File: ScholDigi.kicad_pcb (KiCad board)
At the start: 2 copper layers, 66 x 49 mm, 65 parts, among them J1 Conn_01x04, J2 USB_C_Receptacle_USB2.0_14P, J3 Battery JST, J4 GPS Antenna coaxial, J5 USB_C_Receptacle_USB2.0_14P, Q1 FS8205A, SW1 Boot Button, SW2 Reset Button, U1 ESP32-C6-MINI-1, U2 MAX-M10S, U3 TP4056-42-ESOP8, U4 DW01A, U5 TPS63060, U6 CP2102

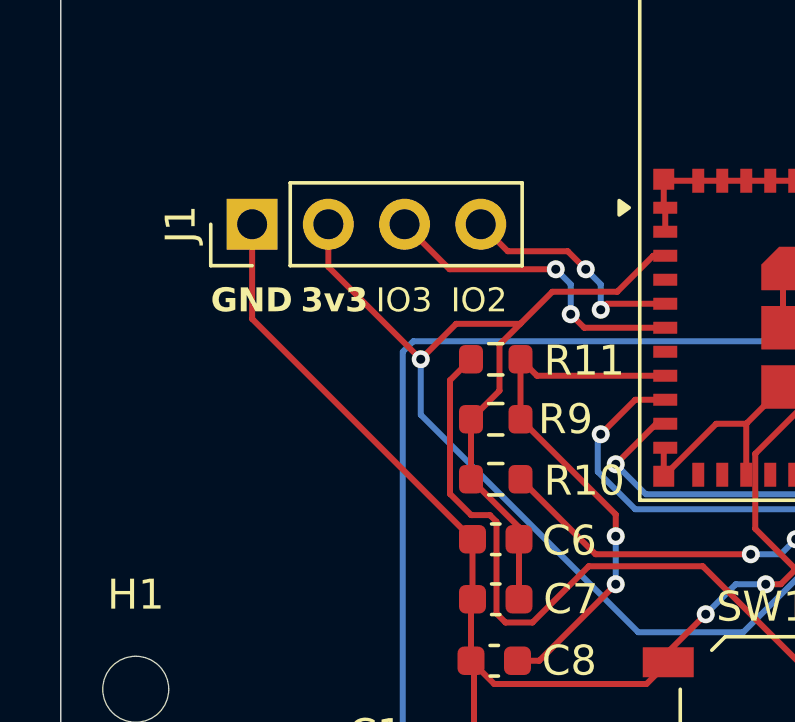
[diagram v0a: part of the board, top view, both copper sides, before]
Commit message: Display header are now through hole solders
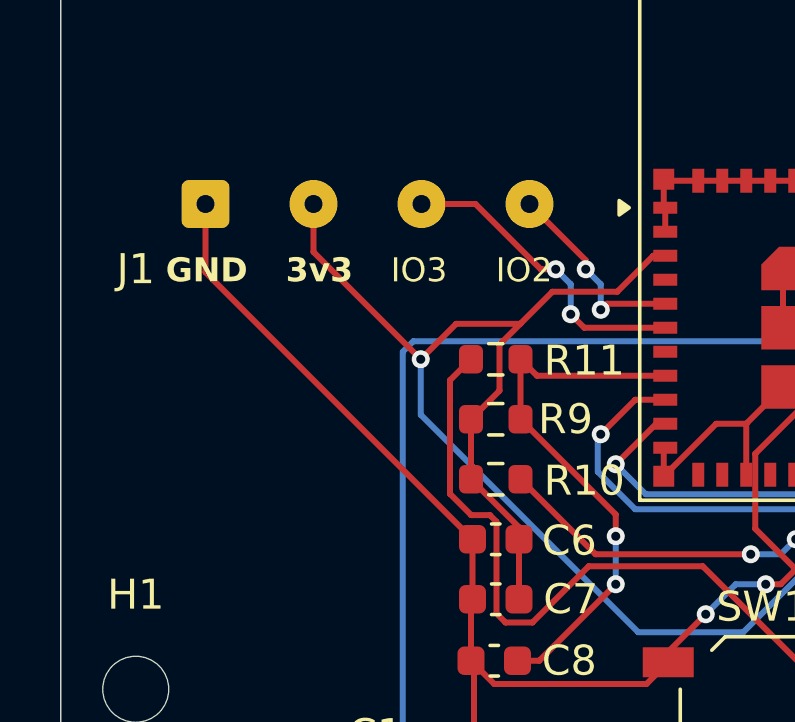
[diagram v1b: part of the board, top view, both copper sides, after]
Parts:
- J1: footprint Connector_PinHeader_2.54mm:PinHeader_1x04_P2.54mm_Vertical -> Connector_Wire:SolderWire-0.1sqmm_1x04_P3.6mm_D0.4mm_OD1mm
- moved J1 1.70 mm to (95.8, 59.3), turned to 0 degrees
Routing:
- net VIN-: track 345.2 -> 346.5 mm
- net IO2: track 7.91 -> 6.74 mm
- net +3V3: track 106.5 -> 107.4 mm

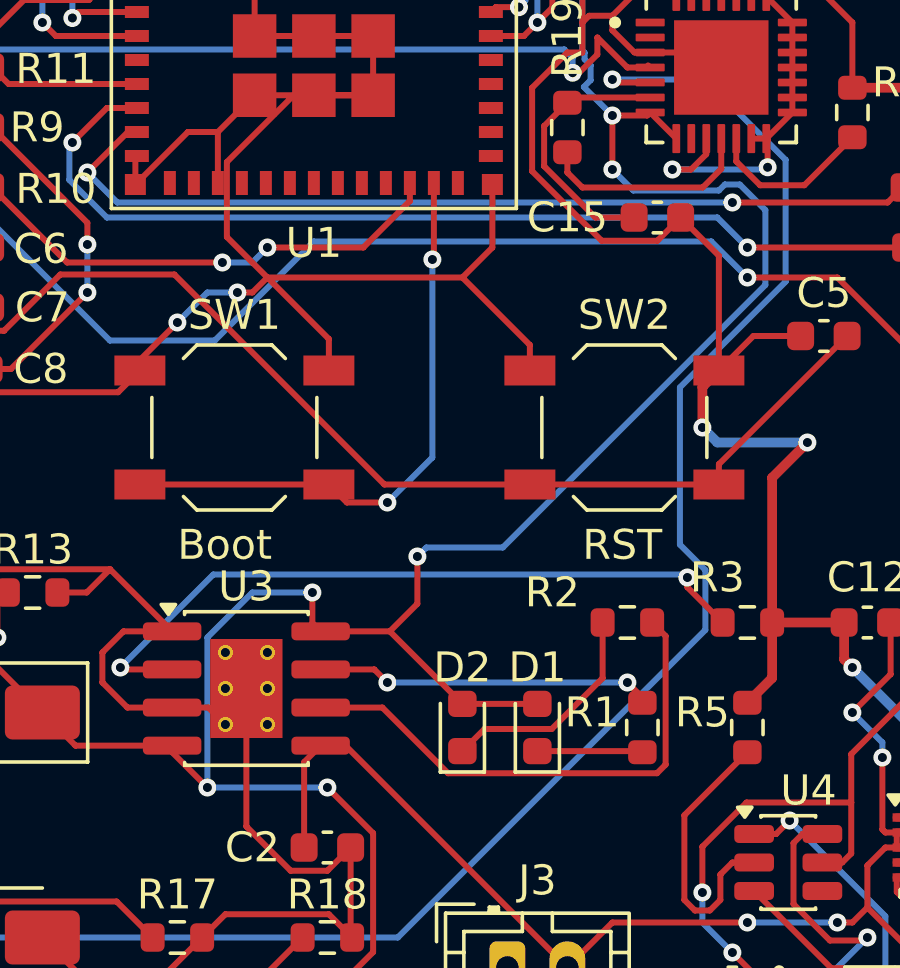
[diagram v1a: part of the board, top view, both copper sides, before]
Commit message: CHanges so that i can get battery voltage
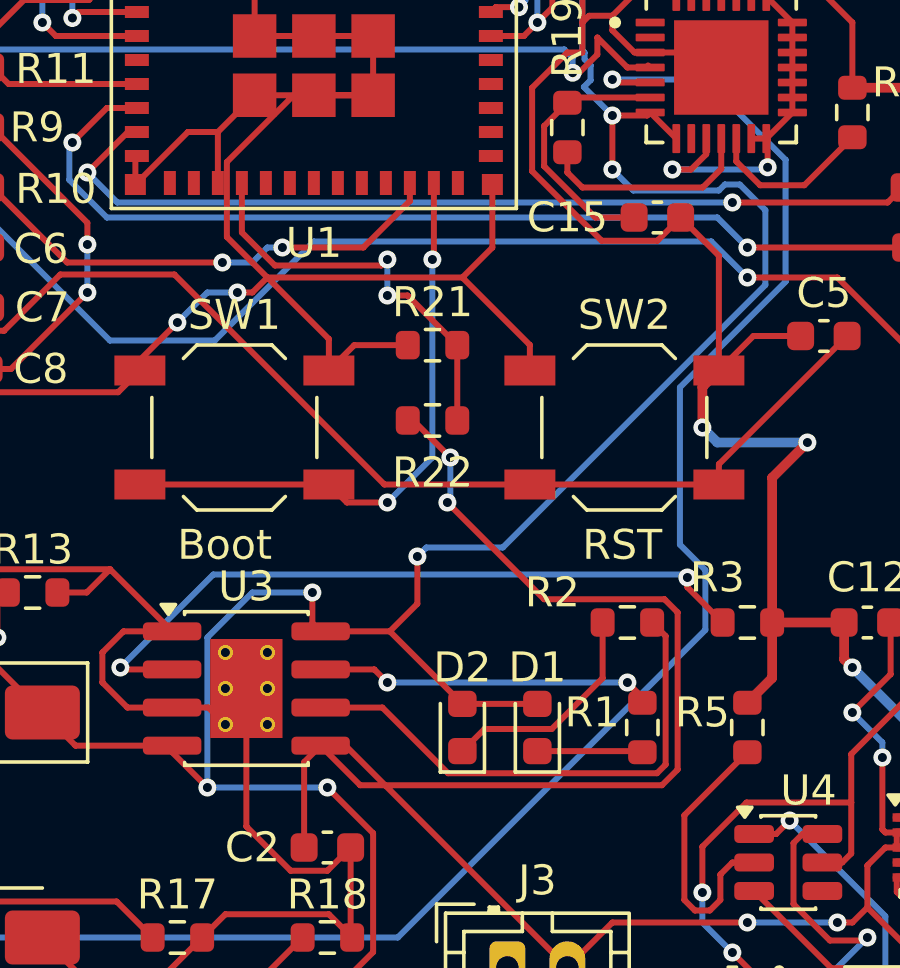
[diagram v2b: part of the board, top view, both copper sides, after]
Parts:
- added R21: 90K, Resistor_SMD:R_0603_1608Metric, F.Cu at (121.0, 73.8)
- added R22: 10K, Resistor_SMD:R_0603_1608Metric, F.Cu at (121.0, 76.3)
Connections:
- U1 pad 15: unconnected-(U1-IO6-Pad15) -> Net-(U1-IO6)
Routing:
- net BAT+: track 53.2 -> 83.8 mm, vias 4 -> 6
- net Net-(U1-IO6): track 0.00 -> 13.8 mm, vias 0 -> 2
- net VIN-: track 346.5 -> 349.5 mm

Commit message: rah
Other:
- board text added: "Anything can be a smoke machine if you try hard enough"
- board text added: "Now with 50% more magic smoke"
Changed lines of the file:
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@@
 		)
 	)
+	(gr_text "Now with 50% more magic smoke"
+		(at 121 64 0)
+		(layer "B.SilkS")
+		(effects
+			(font
+				(size 1.15 1.15)
+				(thickness 0.1)
+			)
+			(justify left bottom mirror)
+		)
+	)
+	(gr_text "Anything can be a smoke machine if you try hard enough"
+		(at 150 100.5 0)
+		(layer "B.SilkS")
+		(effects
+			(font
+				(size 1.25 1.25)
+				(thickness 0.1)
+			)
+			(justify left bottom mirror)
+		)
+	)
 	(segment
 		(start 103.565256 84)
@@
 	)
 	(segment
+		(start 120.175 72.1)
+		(end 119.5 72.1)
+		(width 0.2)
+		(layer "F.Cu")
+		(net "Net-(U1-IO6)")
+	)
+	(segment
+		(start 119.3 71.1)
+		(end 115.751471 71.1)
+		(width 0.2)
+		(layer "F.Cu")
+		(net "Net-(U1-IO6)")
+	)
+	(segment
+		(start 121.83 73.755)
+		(end 121.83 76.265)
+		(width 0.2)
+		(layer "F.Cu")
+		(net "Net-(U1-IO6)")
+	)
+	(segment
+		(start 121.83 73.755)
+		(end 120.175 72.1)
+		(width 0.2)
+		(layer "F.Cu")
+		(net "Net-(U1-IO6)")
+	)
+	(segment
+		(start 114.65 69.998529)
+		(end 114.65 68.35)
+		(width 0.2)
+		(layer "F.Cu")
+		(net "Net-(U1-IO6)")
+	)
+	(segment
+		(start 119.5 70.9)
+		(end 119.3 71.1)
+		(width 0.2)
+		(layer "F.Cu")
+		(net "Net-(U1-IO6)")
+	)
+	(segment
+		(start 115.751471 71.1)
+		(end 114.65 69.998529)
+		(width 0.2)
+		(layer "F.Cu")
+		(net "Net-(U1-IO6)")
+	)
+	(via
+		(at 119.5 72.1)
+		(size 0.6)
+		(drill 0.3)
+		(layers "F.Cu" "B.Cu")
+		(net "Net-(U1-IO6)")
+	)
+	(via
+		(at 119.5 70.9)
+		(size 0.6)
+		(drill 0.3)
+		(layers "F.Cu" "B.Cu")
+		(net "Net-(U1-IO6)")
+	)
+	(segment
+		(start 119.5 72.1)
+		(end 119.5 70.9)
+		(width 0.2)
+		(layer "B.Cu")
+		(net "Net-(U1-IO6)")
+	)
+	(segment
 		(start 128.225 60)
 		(end 127 60)
@@
 		(net "unconnected-(J2-SHIELD-PadSH)")
 	)
-	(segment
-		(start 120.175 72.1)
-		(end 119.5 72.1)
-		(width 0.2)
-		(layer "F.Cu")
-		(net "Net-(U1-IO6)")
-	)
-	(segment
-		(start 119.3 71.1)
-		(end 115.751471 71.1)
-		(width 0.2)
-		(layer "F.Cu")
-		(net "Net-(U1-IO6)")
-	)
-	(segment
-		(start 121.83 73.755)
-		(end 121.83 76.265)
-		(width 0.2)
-		(layer "F.Cu")
-		(net "Net-(U1-IO6)")
-	)
-	(segment
-		(start 121.83 73.755)
-		(end 120.175 72.1)
-		(width 0.2)
-		(layer "F.Cu")
-		(net "Net-(U1-IO6)")
-	)
-	(segment
-		(start 114.65 69.998529)
-		(end 114.65 68.35)
-		(width 0.2)
-		(layer "F.Cu")
-		(net "Net-(U1-IO6)")
-	)
-	(segment
-		(start 119.5 70.9)
-		(end 119.3 71.1)
-		(width 0.2)
-		(layer "F.Cu")
-		(net "Net-(U1-IO6)")
-	)
-	(segment
-		(start 115.751471 71.1)
-		(end 114.65 69.998529)
-		(width 0.2)
-		(layer "F.Cu")
-		(net "Net-(U1-IO6)")
-	)
-	(via
-		(at 119.5 72.1)
-		(size 0.6)
-		(drill 0.3)
-		(layers "F.Cu" "B.Cu")
-		(net "Net-(U1-IO6)")
-	)
-	(via
-		(at 119.5 70.9)
-		(size 0.6)
-		(drill 0.3)
-		(layers "F.Cu" "B.Cu")
-		(net "Net-(U1-IO6)")
-	)
-	(segment
-		(start 119.5 72.1)
-		(end 119.5 70.9)
-		(width 0.2)
-		(layer "B.Cu")
-		(net "Net-(U1-IO6)")
-	)
 	(embedded_fonts no)

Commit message: add funnies
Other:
- board text added: "Any sufficiently advanced technology is indistinguishable from magic - Arthur C Clark"
- board text added: "BAT"
- board text added: "Hi Pookie <3"
- board text added: "It is by pure will alone I set myself to this task"
- board text added: "Made in China"
- board text added: "Peekabooo"
- board text added: "Pineapple on pizza is gods creation"
- board text added: "Please do not the cat."
- board text added: "Remove before flight."
- board text added: "Schrödinger's PCB"
- board text added: "[Verse 1: David Gilmour] Ticking away The moments that make up a dull day You fritter and waste the hours In an offhand way Kicking around on a piece of ground In your hometown Waiting for someone Or something to show you the way [Chorus: Richard Wright] Tired of lying in the sunshine Staying home to watch the rain You are young and life is long And there is time to kill today And then one day yo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"
- board text added: "Привіт світ"
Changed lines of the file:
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@@
+		)
+	)
+	(gr_text "BAT"
+		(at 123 99.5 0)
+		(layer "F.SilkS")
+		(effects
+			(font
+				(size 1 1)
+				(thickness 0.1)
+			)
+			(justify left bottom)
 		)
 	)
@@
 		)
 	)
+	(gr_text "[Verse 1: David Gilmour]\nTicking away\nThe moments that make up a dull day\nYou fritter and waste the hours\nIn an offhand way\nKicking around on a piece of ground\nIn your hometown\nWaiting for someone\nOr something to show you the way\n\n[Chorus: Richard Wright]\nTired of lying in the sunshine\nStaying home to watch the rain\nYou are young and life is long\nAnd there is time to kill today\nAnd then one day you find\nTen years have got behind you\nNo one told you when to run\nYou missed the starting gun\nYou might also like\nmeet the grahams\nKendrick Lamar\nEclipse\nPink Floyd\nTHE HEART PART 6\nDrake\n[Guitar Solo]\n\n[Verse 2: David Gilmour]\nAnd you run, and you run\nTo catch up with the sun, but it's sinking\nAnd racing around\nTo come up behind you again\nThe sun is the same in a relative way\nBut you're older\nShorter of breath\nAnd one day closer to death\n\n[Chorus: Richard Wright]\nEvery year is getting shorter\nNever seem to find the time\nPlans that either come to naught\nOr half a page of scribbled lines\nHanging on in quiet desperation\nIs the English way\nThe time is gone, the song is over\nThought I'd something more to say\n\n[Part II: Breathe (In the Air) [Reprise]]\n\n[Verse: David Gilmour]\nHome, home again\nI like to be here when I can\nWhen I come home cold and tired\nIt's good to warm my bones beside the fire\nFar away across the field\nThe tolling of the iron bell\nCalls the faithful to their knees\nTo hear the softly spoken magic spells"
+		(at 140.5 58.5 90)
+		(layer "B.SilkS")
+		(effects
+			(font
+				(size 0.3 0.3)
+				(thickness 0.02)
+			)
+			(justify left bottom mirror)
+		)
+	)
+	(gr_text "Any sufficiently advanced technology is indistinguishable from magic - Arthur C Clark"
+		(at 154.5 69.5 0)
+		(layer "B.SilkS")
+		(effects
+			(font
+				(size 0.8 0.8)
+				(thickness 0.1)
+			)
+			(justify left bottom mirror)
+		)
+	)
+	(gr_text "Привіт світ"
+		(at 92.5 63.5 90)
+		(layer "B.SilkS")
+		(effects
+			(font
+				(size 0.8 0.8)
+				(thickness 0.1)
+			)
+			(justify left bottom mirror)
+		)
+	)
+	(gr_text "Made in China"
+		(at 127.4 76.5 0)
+		(layer "B.SilkS")
+		(effects
+			(font
+				(size 1 1)
+				(thickness 0.1)
+			)
+			(justify left bottom mirror)
+		)
+	)
+	(gr_text "Pineapple on pizza is gods creation"
+		(at 130 71.5 0)
+		(layer "B.SilkS")
+		(effects
+			(font
+				(size 1 1)
+				(thickness 0.1)
+			)
+			(justify left bottom mirror)
+		)
+	)
+	(gr_text "It is by pure will alone\nI set myself to this task"
+		(at 149 78.5 0)
+		(layer "B.SilkS")
+		(effects
+			(font
+				(size 1 1)
+				(thickness 0.1)
+			)
+			(justify left bottom mirror)
+		)
+	)
+	(gr_text "Hi Pookie <3"
+		(at 151.5 55.5 0)
+		(layer "B.SilkS")
+		(effects
+			(font
+				(size 1 1)
+				(thickness 0.1)
+			)
+			(justify left bottom mirror)
+		)
+	)
+	(gr_text "Peekabooo"
+		(at 99.5 76.5 90)
+		(layer "B.SilkS")
+		(effects
+			(font
+				(size 1 1)
+				(thickness 0.1)
+			)
+			(justify left bottom mirror)
+		)
+	)
+	(gr_text "Schrödinger's PCB"
+		(at 112.5 74 0)
+		(layer "B.SilkS")
+		(effects
+			(font
+				(size 1 1)
+				(thickness 0.15)
+			)
+			(justify left bottom mirror)
+		)
+	)
 	(gr_text "Now with 50% more magic smoke"
-		(at 121 64 0)
+		(at 96.5 63 90)
 		(layer "B.SilkS")
 		(effects
@@
 				(size 1.15 1.15)
 				(thickness 0.1)
+			)
+			(justify left bottom mirror)
+		)
+	)
+	(gr_text "Please do not the cat."
+		(at 153.5 87.5 0)
+		(layer "B.SilkS")
+		(effects
+			(font
+				(size 1.2 1.2)
+				(thickness 0.15)
 			)
 			(justify left bottom mirror)
@@
 			)
 			(justify left bottom mirror)
+		)
+	)
+	(gr_text "Remove before flight."
+		(at 134 91 0)
+		(layer "B.SilkS")
+		(effects
+			(font
+				(size 2 2)
+				(thickness 0.2)
+			)
+			(justify left bottom mirror)

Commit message: Changes to fix DRC
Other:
- board text removed: "[Verse 1: David Gilmour] Ticking away The moments that make up a dull day You fritter and waste the hours In an offhand way Kicking around on a piece of ground In your hometown Waiting for someone Or something to show you the way [Chorus: Richard Wright] Tired of lying in the sunshine Staying home to watch the rain You are young and life is long And there is time to kill today And then one day yo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"
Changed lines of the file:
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@@
-		)
-	)
-	(gr_text "[Verse 1: David Gilmour]\nTicking away\nThe moments that make up a dull day\nYou fritter and waste the hours\nIn an offhand way\nKicking around on a piece of ground\nIn your hometown\nWaiting for someone\nOr something to show you the way\n\n[Chorus: Richard Wright]\nTired of lying in the sunshine\nStaying home to watch the rain\nYou are young and life is long\nAnd there is time to kill today\nAnd then one day you find\nTen years have got behind you\nNo one told you when to run\nYou missed the starting gun\nYou might also like\nmeet the grahams\nKendrick Lamar\nEclipse\nPink Floyd\nTHE HEART PART 6\nDrake\n[Guitar Solo]\n\n[Verse 2: David Gilmour]\nAnd you run, and you run\nTo catch up with the sun, but it's sinking\nAnd racing around\nTo come up behind you again\nThe sun is the same in a relative way\nBut you're older\nShorter of breath\nAnd one day closer to death\n\n[Chorus: Richard Wright]\nEvery year is getting shorter\nNever seem to find the time\nPlans that either come to naught\nOr half a page of scribbled lines\nHanging on in quiet desperation\nIs the English way\nThe time is gone, the song is over\nThought I'd something more to say\n\n[Part II: Breathe (In the Air) [Reprise]]\n\n[Verse: David Gilmour]\nHome, home again\nI like to be here when I can\nWhen I come home cold and tired\nIt's good to warm my bones beside the fire\nFar away across the field\nThe tolling of the iron bell\nCalls the faithful to their knees\nTo hear the softly spoken magic spells"
-		(at 140.5 58.5 90)
-		(layer "B.SilkS")
-		(effects
-			(font
-				(size 0.3 0.3)
-				(thickness 0.02)
-			)
-			(justify left bottom mirror)
 		)
 	)
@@
 		)
 	)
+	(gr_text "Anything can be a smoke machine if you try hard enough"
+		(at 150 100.5 0)
+		(layer "B.SilkS")
+		(effects
+			(font
+				(size 1 1)
+				(thickness 0.1)
+			)
+			(justify left bottom mirror)
+		)
+	)
 	(gr_text "Hi Pookie <3"
 		(at 151.5 55.5 0)
@@
 	)
 	(gr_text "Peekabooo"
-		(at 99.5 76.5 90)
+		(at 98 68.5 90)
 		(layer "B.SilkS")
 		(effects
@@
 			)
 			(justify left bottom mirror)
-		)
-	)
-	(gr_text "Anything can be a smoke machine if you try hard enough"
-		(at 150 100.5 0)
-		(layer "B.SilkS")
-		(effects
-			(font
-				(size 1.25 1.25)
-				(thickness 0.1)
-			)
-			(justify left bottom mirror)
